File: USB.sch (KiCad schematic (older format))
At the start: 53 parts, among them J1 USB_C_Receptacle, J7 USB_MICRO_B, U1 IMX8MM, U11 AP2411SN-7, U2 CYPD4155-96BZXI, U6 SN65DSI86ZQER, U9 NX20P3483UK

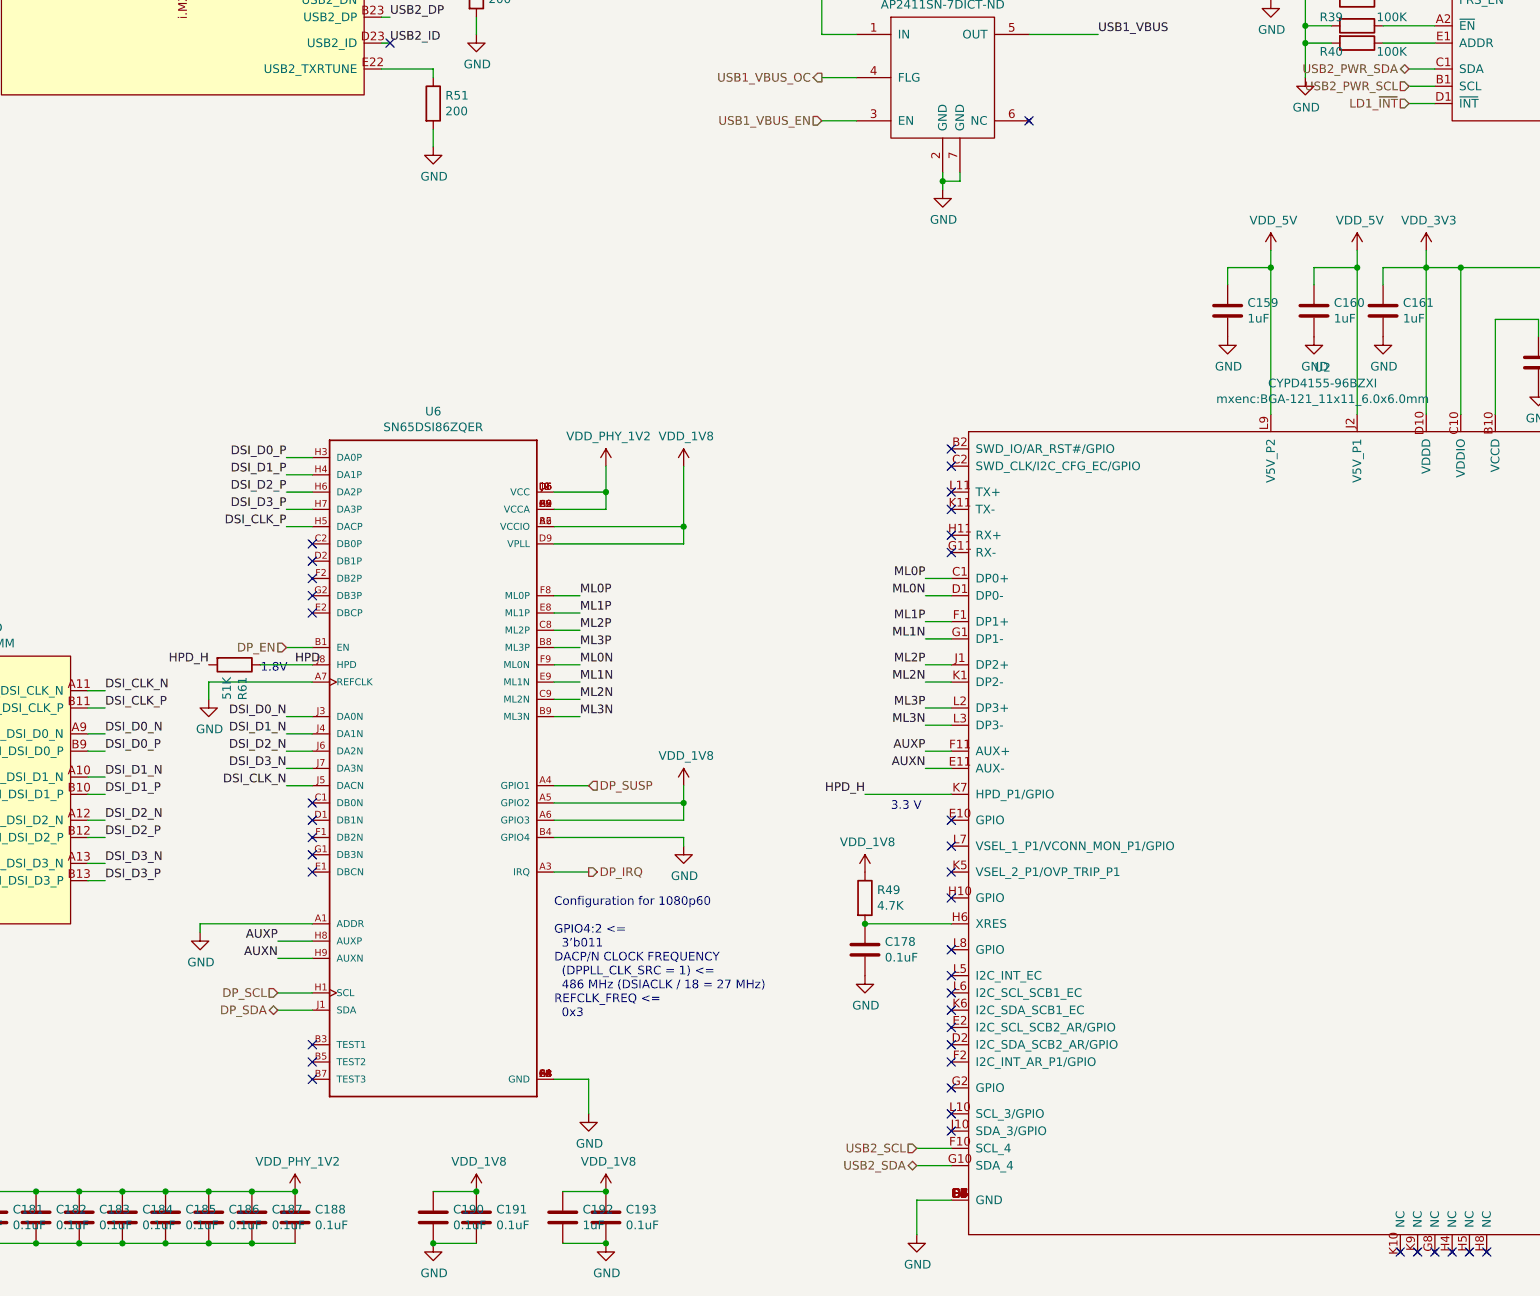
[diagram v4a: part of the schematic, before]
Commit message: Corrections for bom of v0.1
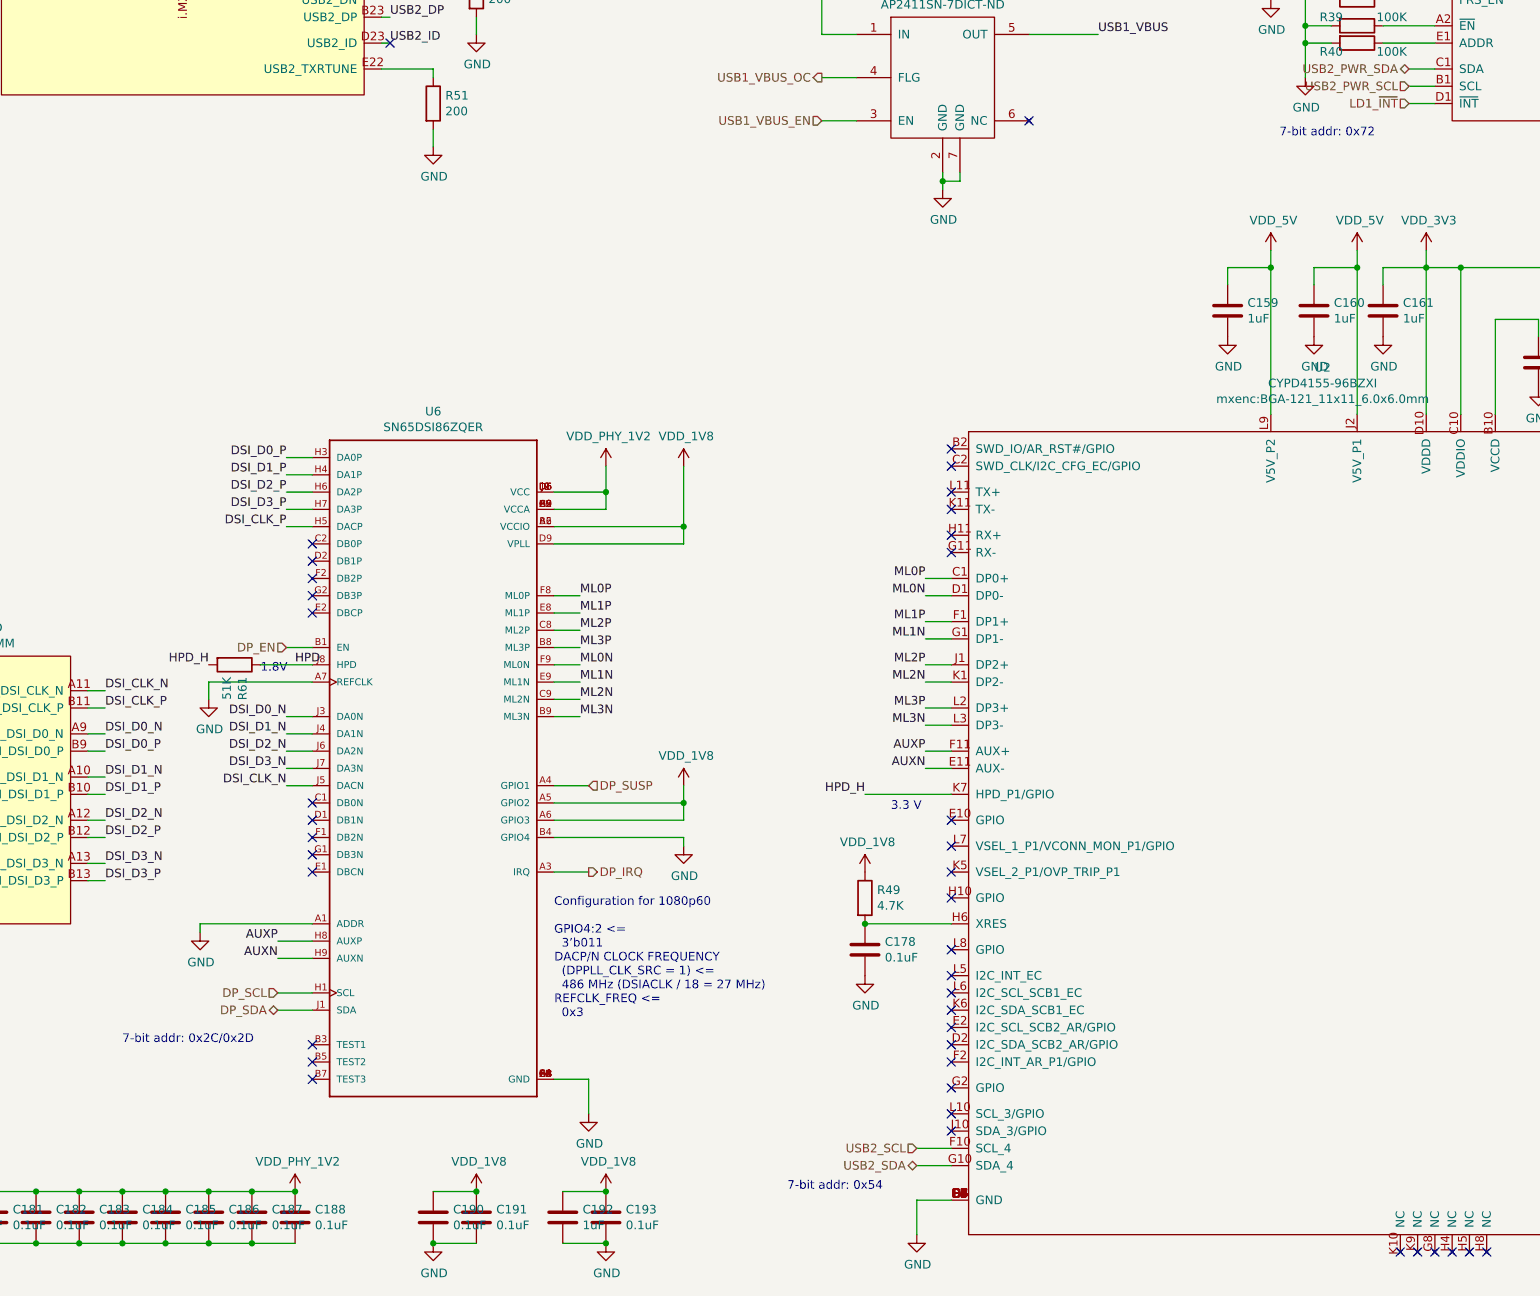
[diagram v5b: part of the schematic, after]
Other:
- note added: "7-bit addr: 0x2C/0x2D"
- note added: "7-bit addr: 0x54"
- note added: "7-bit addr: 0x72"
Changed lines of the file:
@@
 	0    1    1    0
 $EndComp
+Text Notes 2400 8900 0    50   ~ 0
+7-bit addr: 0x2C/0x2D
+Text Notes 6250 9750 0    50   ~ 0
+7-bit addr: 0x54
+Text Notes 9100 3650 0    50   ~ 0
+7-bit addr: 0x72
 $EndSCHEMATC
